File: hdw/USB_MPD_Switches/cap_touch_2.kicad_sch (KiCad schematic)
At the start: 44 parts

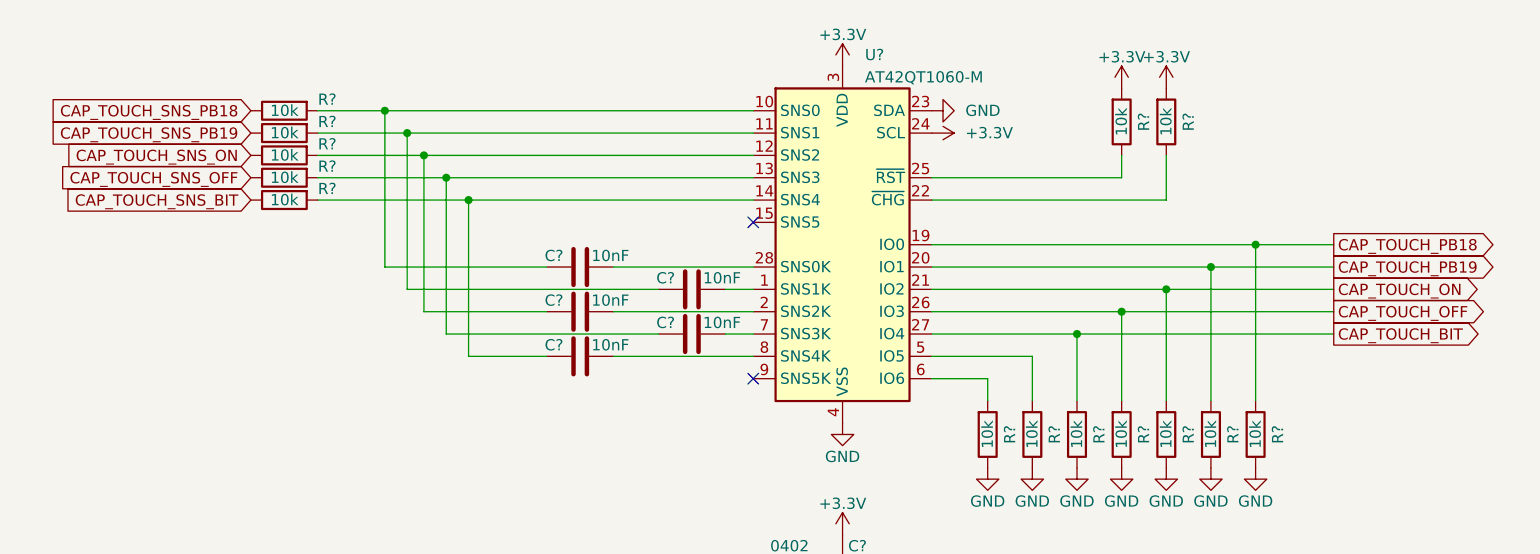
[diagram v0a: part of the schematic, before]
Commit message: added USB port, +3.3V power supply
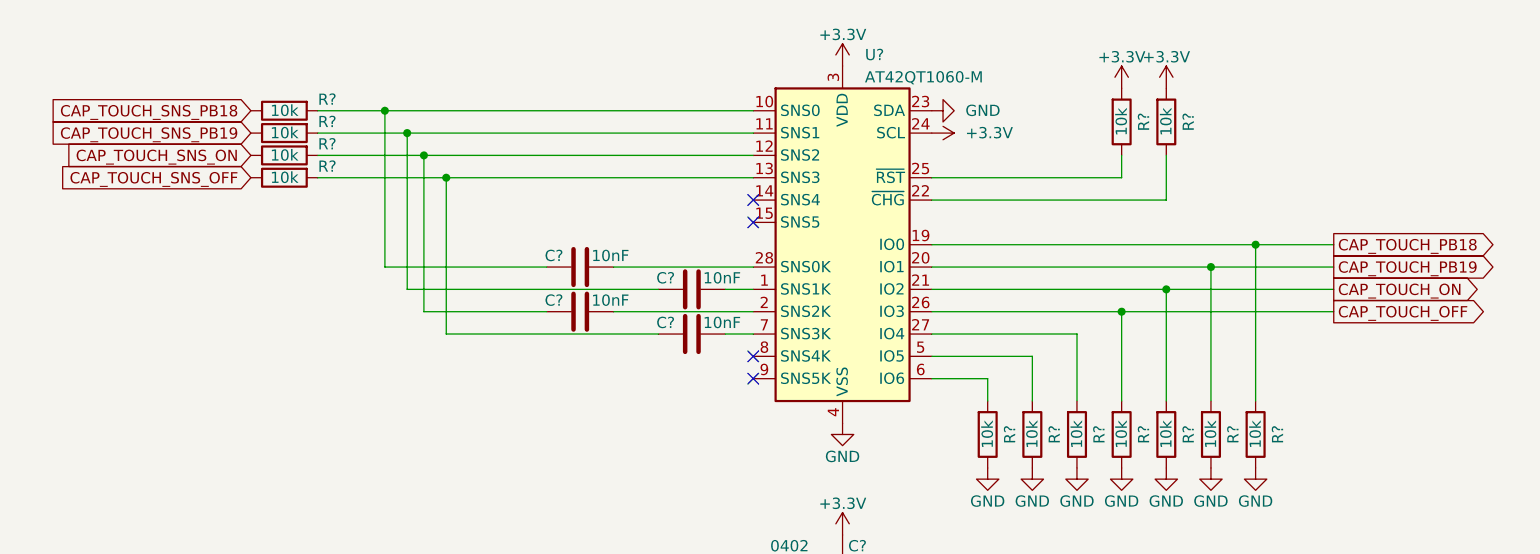
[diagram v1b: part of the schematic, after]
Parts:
- removed C?: 10nF, symbol Custom Library:C_Custom
- removed R?: 10k, symbol Custom_Library:R_Custom
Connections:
- net CAP_TOUCH_BIT: no longer names the net of R?.1, U?.27 (IO4)
- no-connect marks 2 -> 4
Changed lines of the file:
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@@
   (title_block
     (title "USB MPD")
-    (date "2024-02-01")
+    (date "2024-02-06")
     (rev "PRELIM")
     (company "Drew Maatman")
   )
-  (junction (at 166.37 132.08) (diameter 0) (color 0 0 0 0)
-  )
   (junction (at 90.17 33.02) (diameter 0) (color 0 0 0 0)
   )
@@
   (junction (at 97.155 40.64) (diameter 0) (color 0 0 0 0)
   )
-  (junction (at 97.155 116.84) (diameter 0) (color 0 0 0 0)
-  )
+  (no_connect (at 129.54 116.84))
   (no_connect (at 129.54 119.38))
   (no_connect (at 129.54 137.16))
+  (no_connect (at 129.54 134.62))
   (wire (pts (xy 166.37 132.08) (xy 166.37 139.7))
     (stroke (width 0) (type default))
@@
     (stroke (width 0) (type default))
   )
-  (wire (pts (xy 166.37 132.08) (xy 195.58 132.08))
-    (stroke (width 0) (type default))
-  )
   (wire (pts (xy 181.61 124.46) (xy 195.58 124.46))
     (stroke (width 0) (type default))
@@
     (stroke (width 0) (type default))
   )
-  (wire (pts (xy 97.155 116.84) (xy 129.54 116.84))
-    (stroke (width 0) (type default))
-  )
   (wire (pts (xy 161.29 134.62) (xy 161.29 139.7))
     (stroke (width 0) (type default))
@@
     (stroke (width 0) (type default))
   )
-  (wire (pts (xy 97.155 116.84) (xy 97.155 134.62))
-    (stroke (width 0) (type default))
-  )
   (wire (pts (xy 186.69 121.92) (xy 186.69 139.7))
     (stroke (width 0) (type default))
@@
     (stroke (width 0) (type default))
   )
-  (wire (pts (xy 80.01 116.84) (xy 97.155 116.84))
-    (stroke (width 0) (type default))
-  )
   (wire (pts (xy 186.69 45.72) (xy 186.69 63.5))
     (stroke (width 0) (type default))
@@
     (stroke (width 0) (type default))
   )
-  (wire (pts (xy 106.045 134.62) (xy 97.155 134.62))
-    (stroke (width 0) (type default))
-  )
   (wire (pts (xy 80.01 43.18) (xy 99.695 43.18))
     (stroke (width 0) (type default))
   )
-  (wire (pts (xy 113.665 134.62) (xy 129.54 134.62))
-    (stroke (width 0) (type default))
-  )
   (wire (pts (xy 99.695 60.96) (xy 99.695 43.18))
     (stroke (width 0) (type default))
@@
     )
   )
-  (global_label "CAP_TOUCH_BIT" (shape output) (at 195.58 132.08 0) (fields_autoplaced)
-    (effects (font (size 1.27 1.27)) (justify left))
-    (property "Intersheetrefs" "${INTERSHEET_REFS}" (at 213.1211 132.08 0)
-      (effects (font (size 1.27 1.27)) (justify left) hide)
-    )
-  )
   (global_label "CAP_TOUCH_SNS_ON" (shape input) (at 72.39 111.76 180) (fields_autoplaced)
     (effects (font (size 1.27 1.27)) (justify right))
@@
     )
   )
-  (global_label "CAP_TOUCH_SNS_BIT" (shape input) (at 72.39 116.84 180) (fields_autoplaced)
-    (effects (font (size 1.27 1.27)) (justify right))
-    (property "Intersheetrefs" "${INTERSHEET_REFS}" (at 50.1318 116.84 0)
-      (effects (font (size 1.27 1.27)) (justify right) hide)
-    )
-  )
   (symbol (lib_id "Custom Library:C_Custom") (at 122.555 60.96 90) (unit 1)
     (in_bom yes) (on_board yes) (dnp no)
@@
     )
   )
-  (symbol (lib_id "Custom Library:C_Custom") (at 109.855 134.62 90) (unit 1)
-    (in_bom yes) (on_board yes) (dnp no)
-    (property "Reference" "C?" (at 107.95 133.35 90)
-      (effects (font (size 1.27 1.27)) (justify left))
-    )
-    (property "Value" "10nF" (at 111.125 133.35 90)
-      (effects (font (size 1.27 1.27)) (justify right))
-    )
-    (property "Footprint" "" (at 113.665 133.6548 0)
-      (effects (font (size 1.27 1.27)) hide)
-    )
-    (property "Datasheet" "" (at 107.315 133.985 0)
-      (effects (font (size 1.27 1.27)) hide)
-    )
-    (property "display_footprint" "0402" (at 109.855 125.73 90)
-      (effects (font (size 1.27 1.27)) hide)
-    )
-    (property "Voltage" "50V" (at 109.855 128.27 90)
-      (effects (font (size 1.27 1.27)) hide)
-    )
-    (property "Dielectric" "X7R" (at 109.855 130.81 90)
-      (effects (font (size 1.27 1.27)) hide)
-    )
-    (property "Digi-Key PN" "PN" (at 97.155 123.825 0)
-      (effects (font (size 1.524 1.524)) hide)
-    )
-    (pin "1")
-    (pin "2")
-    (instances
-      (project "USB_MPD_Switches"
-        (path "/62d9a549-2742-4d98-96b6-bf7a87f3799a/5f465d3a-417a-4564-add0-6b5b66c97f64"
-          (reference "C?") (unit 1)
-        )
-        (path "/62d9a549-2742-4d98-96b6-bf7a87f3799a/7cd4e104-c64c-48e4-9211-828159723ee3"
-          (reference "C?") (unit 1)
-        )
-      )
-    )
-  )
   (symbol (lib_id "Custom_Library:R_Custom") (at 186.69 67.31 0) (mirror y) (unit 1)
     (in_bom yes) (on_board yes) (dnp no)
@@
         )
       )
-    )
-  )
-  (symbol (lib_id "Custom_Library:R_Custom") (at 76.2 116.84 270) (mirror x) (unit 1)
-    (in_bom yes) (on_board yes) (dnp no)
-    (property "Reference" "R?" (at 80.01 115.57 90)
-      (effects (font (size 1.27 1.27)) (justify left))
-    )
-    (property "Value" "10k" (at 76.2 116.84 90)
-      (effects (font (size 1.27 1.27)))
-    )
-    (property "Footprint" "" (at 76.2 116.84 0)
-      (effects (font (size 1.27 1.27)) hide)
-    )
-    (property "Datasheet" "" (at 76.2 116.84 0)
-      (effects (font (size 1.27 1.27)) hide)
-    )
-    (property "display_footprint" "0402" (at 78.232 112.014 0)
-      (effects (font (size 1.27 1.27)) hide)
-    )
-    (property "Tolerance" "1%" (at 76.2 112.268 0)
-      (effects (font (size 1.27 1.27)) hide)
-    )
-    (property "Wattage" "1/16W" (at 74.422 111.506 0)
-      (effects (font (size 1.27 1.27)) hide)
-    )
-    (property "Digi-Key PN" "" (at 86.36 109.22 0)
-      (effects (font (size 1.524 1.524)) hide)
-    )
-    (pin "1")
-    (pin "2")
-    (instances
-      (project "Analog_Clock"
-        (path "/0dc9b974-a945-4291-bc55-04b8e342b0e5/00000000-0000-0000-0000-00005baae1dc"
-          (reference "R?") (unit 1)
-        )
-        (path "/0dc9b974-a945-4291-bc55-04b8e342b0e5/00000000-0000-0000-0000-00005c1d5cb6"
-          (reference "R?") (unit 1)
-        )
-        (path "/0dc9b974-a945-4291-bc55-04b8e342b0e5/00000000-0000-0000-0000-00005e697920"
-          (reference "R?") (unit 1)
-        )
-        (path "/0dc9b974-a945-4291-bc55-04b8e342b0e5/00000000-0000-0000-0000-00005e939eaf"
-          (reference "R?") (unit 1)
-        )
-        (path "/0dc9b974-a945-4291-bc55-04b8e342b0e5/00000000-0000-0000-0000-00005baae16c"
-          (reference "R?") (unit 1)
-        )
-        (path "/0dc9b974-a945-4291-bc55-04b8e342b0e5/00000000-0000-0000-0000-00005eae2ef2"
-          (reference "R?") (unit 1)
-        )
-        (path "/0dc9b974-a945-4291-bc55-04b8e342b0e5/00000000-0000-0000-0000-00005cb0bc26"
-          (reference "R?") (unit 1)
-        )
-        (path "/0dc9b974-a945-4291-bc55-04b8e342b0e5/00000000-0000-0000-0000-00005baae1f3"
-          (reference "R?") (unit 1)
-        )
-      )
-      (project "Nixie_Clock_Core"
-        (path "/16fdce21-b570-4d81-a458-e8839d611806/0953f70f-0c64-48c1-b5cf-d1f41f95ef1f"
-          (reference "R804") (unit 1)
-        )
-      )
-      (project "USB_MPD_Switches"
-        (path "/62d9a549-2742-4d98-96b6-bf7a87f3799a/abc131ef-9232-4c48-9a74-f81897d40aea"
-          (reference "R?") (unit 1)
-        )
-        (path "/62d9a549-2742-4d98-96b6-bf7a87f3799a/c52f335e-c051-4bb5-99cb-33379bf7e677"
-          (reference "R?") (unit 1)
-        )
-        (path "/62d9a549-2742-4d98-96b6-bf7a87f3799a/5f465d3a-417a-4564-add0-6b5b66c97f64"
-          (reference "R?") (unit 1)
-        )
-        (path "/62d9a549-2742-4d98-96b6-bf7a87f3799a/7cd4e104-c64c-48e4-9211-828159723ee3"
-          (reference "R?") (unit 1)
-        )
-      )
